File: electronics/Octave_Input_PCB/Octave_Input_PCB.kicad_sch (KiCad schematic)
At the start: 37 parts, among them SW1 SW_Hot_Swap_Socket, SW10 SW_Hot_Swap_Socket, SW11 SW_Hot_Swap_Socket, SW12 SW_Hot_Swap_Socket, SW13 SW_Hot_Swap_Socket, SW14 Alps_Alpine_RKJXV1224, SW15 Bourns_PEC12R-4xxxF-Sxxx, SW2 SW_Hot_Swap_Socket, SW3 SW_Hot_Swap_Socket, SW4 SW_Hot_Swap_Socket, SW5 SW_Hot_Swap_Socket, SW6 SW_Hot_Swap_Socket, SW7 SW_Hot_Swap_Socket, SW8 SW_Hot_Swap_Socket, SW9 SW_Hot_Swap_Socket, U1 Adafruit_QT_Py_RP2040

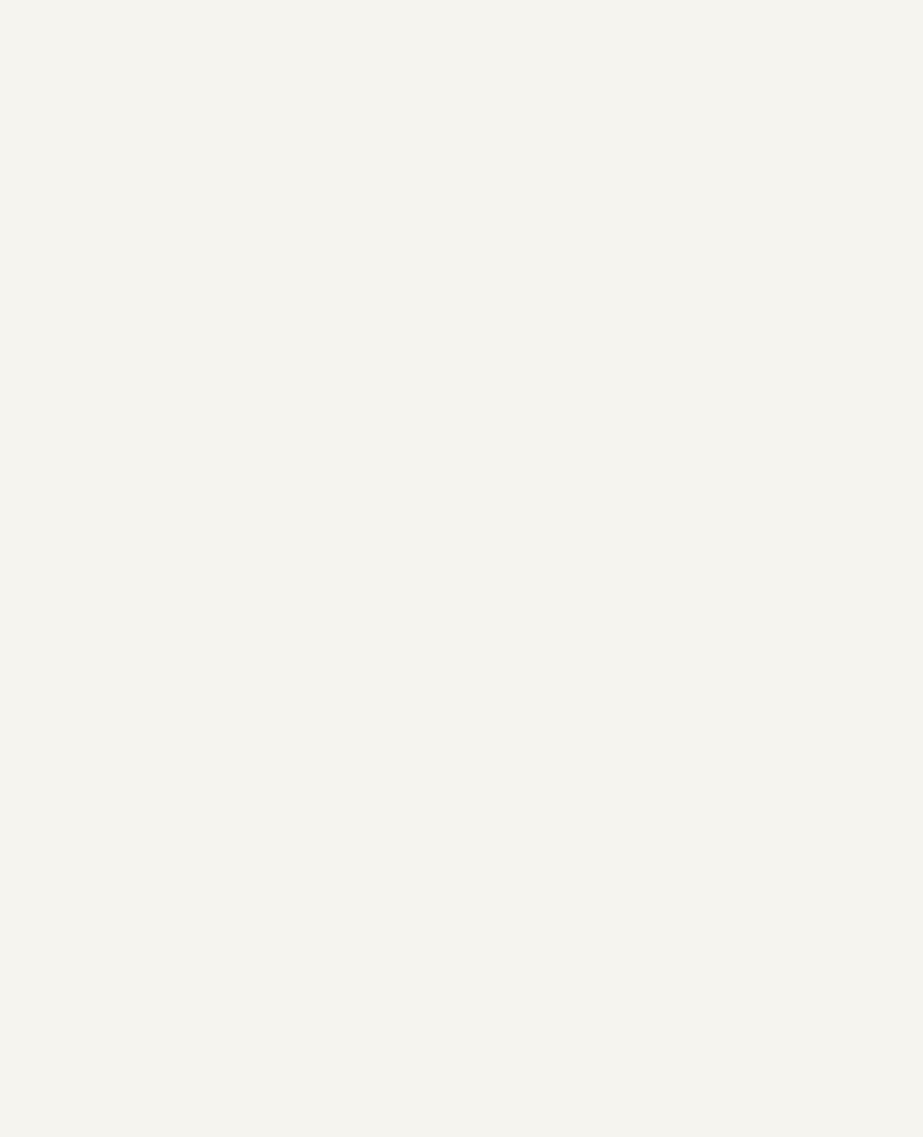
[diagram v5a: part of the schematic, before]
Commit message: Add RP2040 #schematic
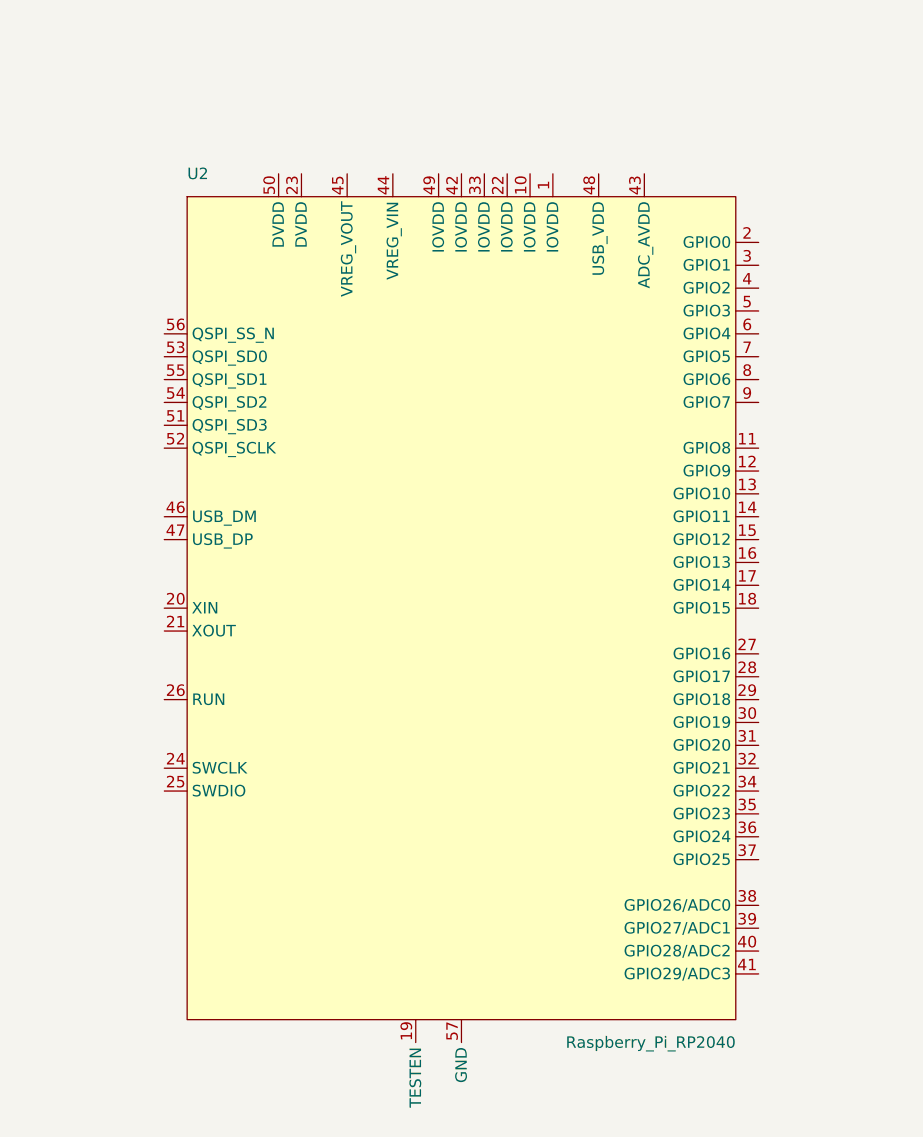
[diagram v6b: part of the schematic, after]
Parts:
- added U2: Raspberry_Pi_RP2040, Octave_Library:RP2040_QFN-56, symbol Octave_Library:Raspberry_Pi_RP2040
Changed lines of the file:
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@@
   (title_block
     (title "Octave - Input PCB")
-    (date "2022-04-29")
-    (rev "4")
+    (date "2022-05-04")
+    (rev "5.a")
     (comment 4 "https://github.com/takayoshiotake/octave-12-key-macropad")
   )
@@
   (symbol (lib_id "power:+3.3V") (at 223.52 110.49 0) (unit 1)
     (in_bom yes) (on_board yes) (fields_autoplaced)
-    (property "Reference" "#PWR?" (id 0) (at 223.52 114.3 0)
+    (property "Reference" "#PWR0102" (id 0) (at 223.52 114.3 0)
       (effects (font (size 1.27 1.27)) hide)
     )
@@
     (pin "1")
     (pin "2")
+  )
+  (symbol (lib_id "Octave_Library:Raspberry_Pi_RP2040") (at 92.71 133.35 0) (unit 1)
+    (in_bom yes) (on_board yes)
+    (property "Reference" "U2" (id 0) (at 62.23 85.09 0)
+      (effects (font (size 1.27 1.27)) (justify left))
+    )
+    (property "Value" "Raspberry_Pi_RP2040" (id 1) (at 123.19 181.61 0)
+      (effects (font (size 1.27 1.27)) (justify right))
+    )
+    (property "Footprint" "Octave_Library:RP2040_QFN-56" (id 2) (at 92.71 133.35 0)
+      (effects (font (size 1.27 1.27)) hide)
+    )
+    (property "Datasheet" "" (id 3) (at 92.71 156.21 0)
+      (effects (font (size 1.27 1.27)) hide)
+    )
+    (pin "1")
+    (pin "10")
+    (pin "11")
+    (pin "12")
+    (pin "13")
+    (pin "14")
+    (pin "15")
+    (pin "16")
+    (pin "17")
+    (pin "18")
+    (pin "19")
+    (pin "2")
+    (pin "20")
+    (pin "21")
+    (pin "22")
+    (pin "23")
+    (pin "24")
+    (pin "25")
+    (pin "26")
+    (pin "27")
+    (pin "28")
+    (pin "29")
+    (pin "3")
+    (pin "30")
+    (pin "31")
+    (pin "32")
+    (pin "33")
+    (pin "34")
+    (pin "35")
+    (pin "36")
+    (pin "37")
+    (pin "38")
+    (pin "39")
+    (pin "4")
+    (pin "40")
+    (pin "41")
+    (pin "42")
+    (pin "43")
+    (pin "44")
+    (pin "45")
+    (pin "46")
+    (pin "47")
+    (pin "48")
+    (pin "49")
+    (pin "5")
+    (pin "50")
+    (pin "51")
+    (pin "52")
+    (pin "53")
+    (pin "54")
+    (pin "55")
+    (pin "56")
+    (pin "57")
+    (pin "6")
+    (pin "7")
+    (pin "8")
+    (pin "9")
   )
   (symbol (lib_id "Diode:1N4148WS") (at 180.34 38.1 90) (unit 1)
@@
   (symbol (lib_id "power:GND") (at 218.44 115.57 0) (unit 1)
     (in_bom yes) (on_board yes) (fields_autoplaced)
-    (property "Reference" "#PWR?" (id 0) (at 218.44 121.92 0)
+    (property "Reference" "#PWR0101" (id 0) (at 218.44 121.92 0)
       (effects (font (size 1.27 1.27)) hide)
     )
@@
   (symbol (lib_id "power:+3.3V") (at 195.58 110.49 0) (unit 1)
     (in_bom yes) (on_board yes) (fields_autoplaced)
-    (property "Reference" "#PWR?" (id 0) (at 195.58 114.3 0)
+    (property "Reference" "#PWR0104" (id 0) (at 195.58 114.3 0)
       (effects (font (size 1.27 1.27)) hide)
     )
@@
   (symbol (lib_id "power:GND") (at 200.66 115.57 0) (unit 1)
     (in_bom yes) (on_board yes) (fields_autoplaced)
-    (property "Reference" "#PWR?" (id 0) (at 200.66 121.92 0)
+    (property "Reference" "#PWR0103" (id 0) (at 200.66 121.92 0)
       (effects (font (size 1.27 1.27)) hide)
     )
@@
       (reference "#PWR07") (unit 1) (value "+3.3V") (footprint "")
     )
+    (path "/95c5557f-99eb-4648-bde6-d53e11cf48f1"
+      (reference "#PWR0101") (unit 1) (value "GND") (footprint "")
+    )
     (path "/39e40374-5e2a-443a-8fbe-89eca3b36e7e"
-      (reference "#PWR?") (unit 1) (value "+3.3V") (footprint "")
-    )
-    (path "/95c5557f-99eb-4648-bde6-d53e11cf48f1"
-      (reference "#PWR?") (unit 1) (value "GND") (footprint "")
+      (reference "#PWR0102") (unit 1) (value "+3.3V") (footprint "")
+    )
+    (path "/cfa126e2-1045-4497-be93-6681d5f25665"
+      (reference "#PWR0103") (unit 1) (value "GND") (footprint "")
     )
     (path "/96c46386-d684-40bb-ae69-6b4b3b025797"
-      (reference "#PWR?") (unit 1) (value "+3.3V") (footprint "")
-    )
-    (path "/cfa126e2-1045-4497-be93-6681d5f25665"
-      (reference "#PWR?") (unit 1) (value "GND") (footprint "")
+      (reference "#PWR0104") (unit 1) (value "+3.3V") (footprint "")
     )
     (path "/172c53e1-ff21-4247-8ac3-d08b615ae4b5"
@@
       (reference "U1") (unit 1) (value "Adafruit_QT_Py_RP2040") (footprint "Octave_Library:Adafruit_QT_Py_RP2040")
     )
-  )
+    (path "/68d14432-223b-47bb-bd26-18873cfb3df2"
+      (reference "U2") (unit 1) (value "Raspberry_Pi_RP2040") (footprint "Octave_Library:RP2040_QFN-56")
+    )
+  )

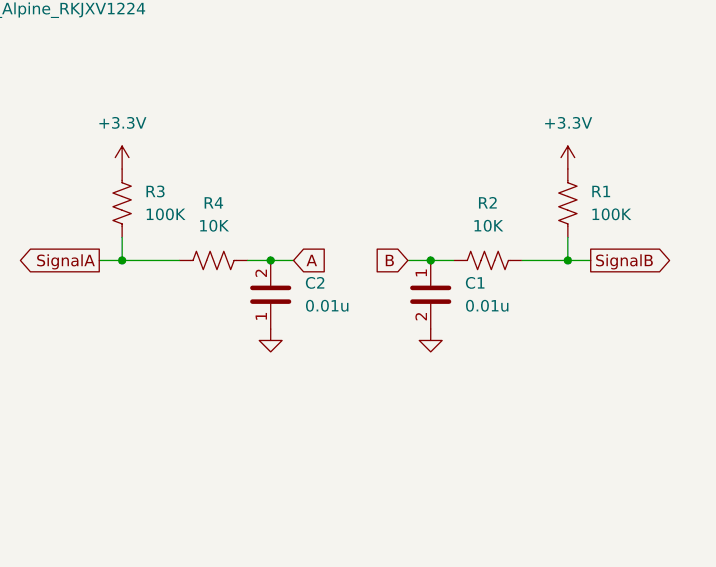
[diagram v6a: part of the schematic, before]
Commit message: Renumber the capacitors #schematic
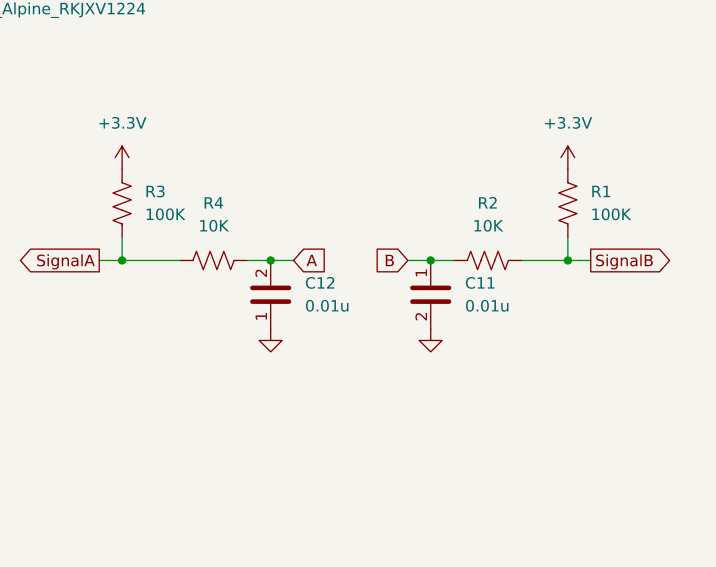
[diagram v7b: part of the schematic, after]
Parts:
- renumbered C1 to C11, C2 to C12
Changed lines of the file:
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@@
   (symbol (lib_name "C_1") (lib_id "Device:C") (at 251.46 153.67 0) (unit 1)
     (in_bom yes) (on_board yes) (fields_autoplaced)
-    (property "Reference" "C1" (id 0) (at 255.27 152.3999 0)
+    (property "Reference" "C11" (id 0) (at 255.27 152.3999 0)
       (effects (font (size 1.27 1.27)) (justify left))
     )
@@
   (symbol (lib_id "Device:C") (at 233.68 153.67 180) (unit 1)
     (in_bom yes) (on_board yes) (fields_autoplaced)
-    (property "Reference" "C2" (id 0) (at 237.49 152.3999 0)
+    (property "Reference" "C12" (id 0) (at 237.49 152.3999 0)
       (effects (font (size 1.27 1.27)) (justify right))
     )
@@
     )
     (path "/172c53e1-ff21-4247-8ac3-d08b615ae4b5"
-      (reference "C1") (unit 1) (value "0.01u") (footprint "Octave_Library:C_0805_2012Metric")
+      (reference "C11") (unit 1) (value "0.01u") (footprint "Octave_Library:C_0805_2012Metric")
     )
     (path "/21ad77bf-5ff1-4e47-a420-889e2c26128b"
-      (reference "C2") (unit 1) (value "0.01u") (footprint "Octave_Library:C_0805_2012Metric")
+      (reference "C12") (unit 1) (value "0.01u") (footprint "Octave_Library:C_0805_2012Metric")
     )
     (path "/709f02fa-f113-4f34-aada-ad74ed9e0d25"

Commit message: Change the diode footprint for the key matrix from SOD-323 to SOD-323F
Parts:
- D1, D10, D11, D12, D13, D14, D15, D2, D3, D4, D5, D6, D7, D8, D9: footprint Octave_Library:D_SOD-323 -> Octave_Library:D_SOD-323F
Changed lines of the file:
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@@
       (effects (font (size 1.27 1.27)) (justify right))
     )
-    (property "Footprint" "Octave_Library:D_SOD-323" (id 2) (at 230.505 55.88 0)
+    (property "Footprint" "Octave_Library:D_SOD-323F" (id 2) (at 230.505 55.88 0)
       (effects (font (size 1.27 1.27)) hide)
     )
@@
       (effects (font (size 1.27 1.27)) (justify right))
     )
-    (property "Footprint" "Octave_Library:D_SOD-323" (id 2) (at 215.265 55.88 0)
+    (property "Footprint" "Octave_Library:D_SOD-323F" (id 2) (at 215.265 55.88 0)
       (effects (font (size 1.27 1.27)) hide)
     )
@@
       (effects (font (size 1.27 1.27)) (justify right))
     )
-    (property "Footprint" "Octave_Library:D_SOD-323" (id 2) (at 184.785 91.44 0)
+    (property "Footprint" "Octave_Library:D_SOD-323F" (id 2) (at 184.785 91.44 0)
       (effects (font (size 1.27 1.27)) hide)
     )
@@
       (effects (font (size 1.27 1.27)) (justify right))
     )
-    (property "Footprint" "Octave_Library:D_SOD-323" (id 2) (at 215.265 38.1 0)
+    (property "Footprint" "Octave_Library:D_SOD-323F" (id 2) (at 215.265 38.1 0)
       (effects (font (size 1.27 1.27)) hide)
     )
@@
       (effects (font (size 1.27 1.27)) (justify right))
     )
-    (property "Footprint" "Octave_Library:D_SOD-323" (id 2) (at 200.025 55.88 0)
+    (property "Footprint" "Octave_Library:D_SOD-323F" (id 2) (at 200.025 55.88 0)
       (effects (font (size 1.27 1.27)) hide)
     )
@@
       (effects (font (size 1.27 1.27)) (justify right))
     )
-    (property "Footprint" "Octave_Library:D_SOD-323" (id 2) (at 200.025 38.1 0)
+    (property "Footprint" "Octave_Library:D_SOD-323F" (id 2) (at 200.025 38.1 0)
       (effects (font (size 1.27 1.27)) hide)
     )
@@
       (effects (font (size 1.27 1.27)) (justify right))
     )
-    (property "Footprint" "Octave_Library:D_SOD-323" (id 2) (at 184.785 55.88 0)
+    (property "Footprint" "Octave_Library:D_SOD-323F" (id 2) (at 184.785 55.88 0)
       (effects (font (size 1.27 1.27)) hide)
     )
@@
       (effects (font (size 1.27 1.27)) (justify right))
     )
-    (property "Footprint" "Octave_Library:D_SOD-323" (id 2) (at 196.215 99.06 0)
+    (property "Footprint" "Octave_Library:D_SOD-323F" (id 2) (at 196.215 99.06 0)
       (effects (font (size 1.27 1.27)) hide)
     )
@@
       (effects (font (size 1.27 1.27)) (justify right))
     )
-    (property "Footprint" "Octave_Library:D_SOD-323" (id 2) (at 200.025 73.66 0)
+    (property "Footprint" "Octave_Library:D_SOD-323F" (id 2) (at 200.025 73.66 0)
       (effects (font (size 1.27 1.27)) hide)
     )
@@
       (effects (font (size 1.27 1.27)) (justify right))
     )
-    (property "Footprint" "Octave_Library:D_SOD-323" (id 2) (at 184.785 38.1 0)
+    (property "Footprint" "Octave_Library:D_SOD-323F" (id 2) (at 184.785 38.1 0)
       (effects (font (size 1.27 1.27)) hide)
     )
@@
       (effects (font (size 1.27 1.27)) (justify right))
     )
-    (property "Footprint" "Octave_Library:D_SOD-323" (id 2) (at 184.785 73.66 0)
+    (property "Footprint" "Octave_Library:D_SOD-323F" (id 2) (at 184.785 73.66 0)
       (effects (font (size 1.27 1.27)) hide)
     )
@@
       (effects (font (size 1.27 1.27)) (justify right))
     )
-    (property "Footprint" "Octave_Library:D_SOD-323" (id 2) (at 230.505 73.66 0)
+    (property "Footprint" "Octave_Library:D_SOD-323F" (id 2) (at 230.505 73.66 0)
       (effects (font (size 1.27 1.27)) hide)
     )
@@
       (effects (font (size 1.27 1.27)) (justify right))
     )
-    (property "Footprint" "Octave_Library:D_SOD-323" (id 2) (at 215.265 73.66 0)
+    (property "Footprint" "Octave_Library:D_SOD-323F" (id 2) (at 215.265 73.66 0)
       (effects (font (size 1.27 1.27)) hide)
     )
@@
       (effects (font (size 1.27 1.27)) (justify right))
     )
-    (property "Footprint" "Octave_Library:D_SOD-323" (id 2) (at 255.905 91.44 0)
+    (property "Footprint" "Octave_Library:D_SOD-323F" (id 2) (at 255.905 91.44 0)
       (effects (font (size 1.27 1.27)) hide)
     )
@@
       (effects (font (size 1.27 1.27)) (justify right))
     )
-    (property "Footprint" "Octave_Library:D_SOD-323" (id 2) (at 230.505 38.1 0)
+    (property "Footprint" "Octave_Library:D_SOD-323F" (id 2) (at 230.505 38.1 0)
       (effects (font (size 1.27 1.27)) hide)
     )
@@
     )
     (path "/709f02fa-f113-4f34-aada-ad74ed9e0d25"
-      (reference "D1") (unit 1) (value "1N4148WS") (footprint "Octave_Library:D_SOD-323")
+      (reference "D1") (unit 1) (value "1N4148WS") (footprint "Octave_Library:D_SOD-323F")
     )
     (path "/3c5d03ad-ef2a-44d3-bc52-83fc5cd731c2"
-      (reference "D2") (unit 1) (value "1N4148WS") (footprint "Octave_Library:D_SOD-323")
+      (reference "D2") (unit 1) (value "1N4148WS") (footprint "Octave_Library:D_SOD-323F")
     )
     (path "/1a8ff821-98c8-41ef-919b-9109469cd4f0"
-      (reference "D3") (unit 1) (value "1N4148WS") (footprint "Octave_Library:D_SOD-323")
+      (reference "D3") (unit 1) (value "1N4148WS") (footprint "Octave_Library:D_SOD-323F")
     )
     (path "/fbe8ce2d-ce37-4567-b78b-14cbdd8d5fa9"
-      (reference "D4") (unit 1) (value "1N4148WS") (footprint "Octave_Library:D_SOD-323")
+      (reference "D4") (unit 1) (value "1N4148WS") (footprint "Octave_Library:D_SOD-323F")
     )
     (path "/4180a1a8-8e9e-403c-882e-e605ec012797"
-      (reference "D5") (unit 1) (value "1N4148WS") (footprint "Octave_Library:D_SOD-323")
+      (reference "D5") (unit 1) (value "1N4148WS") (footprint "Octave_Library:D_SOD-323F")
     )
     (path "/289a3e37-e58b-4925-9d57-18405effc2cb"
-      (reference "D6") (unit 1) (value "1N4148WS") (footprint "Octave_Library:D_SOD-323")
+      (reference "D6") (unit 1) (value "1N4148WS") (footprint "Octave_Library:D_SOD-323F")
     )
     (path "/0e2cc3b9-7e96-4254-8233-44f8db422f6e"
-      (reference "D7") (unit 1) (value "1N4148WS") (footprint "Octave_Library:D_SOD-323")
+      (reference "D7") (unit 1) (value "1N4148WS") (footprint "Octave_Library:D_SOD-323F")
     )
     (path "/053dae26-0d29-4615-8f3a-499ae7356113"
-      (reference "D8") (unit 1) (value "1N4148WS") (footprint "Octave_Library:D_SOD-323")
+      (reference "D8") (unit 1) (value "1N4148WS") (footprint "Octave_Library:D_SOD-323F")
     )
     (path "/764ac2d4-e593-4865-97ff-ed8b82b2353d"
-      (reference "D9") (unit 1) (value "1N4148WS") (footprint "Octave_Library:D_SOD-323")
+      (reference "D9") (unit 1) (value "1N4148WS") (footprint "Octave_Library:D_SOD-323F")
     )
     (path "/58bc63e9-f591-47dd-8596-d72edc57116c"
-      (reference "D10") (unit 1) (value "1N4148WS") (footprint "Octave_Library:D_SOD-323")
+      (reference "D10") (unit 1) (value "1N4148WS") (footprint "Octave_Library:D_SOD-323F")
     )
     (path "/9caea4a2-5bc1-44cc-8293-300131386895"
-      (reference "D11") (unit 1) (value "1N4148WS") (footprint "Octave_Library:D_SOD-323")
+      (reference "D11") (unit 1) (value "1N4148WS") (footprint "Octave_Library:D_SOD-323F")
     )
     (path "/870e1d5b-9785-4c66-8095-64350a305b0a"
-      (reference "D12") (unit 1) (value "1N4148WS") (footprint "Octave_Library:D_SOD-323")
+      (reference "D12") (unit 1) (value "1N4148WS") (footprint "Octave_Library:D_SOD-323F")
     )
     (path "/15dd2ce1-5057-4d96-93de-f9436edad95a"
-      (reference "D13") (unit 1) (value "1N4148WS") (footprint "Octave_Library:D_SOD-323")
+      (reference "D13") (unit 1) (value "1N4148WS") (footprint "Octave_Library:D_SOD-323F")
     )
     (path "/4a30fcaa-fa70-4ef7-bc18-1d232fee7d95"
-      (reference "D14") (unit 1) (value "1N4148WS") (footprint "Octave_Library:D_SOD-323")
+      (reference "D14") (unit 1) (value "1N4148WS") (footprint "Octave_Library:D_SOD-323F")
     )
     (path "/fbc0e23d-9856-4676-a4d7-95fcc2785fe2"
-      (reference "D15") (unit 1) (value "1N4148WS") (footprint "Octave_Library:D_SOD-323")
+      (reference "D15") (unit 1) (value "1N4148WS") (footprint "Octave_Library:D_SOD-323F")
     )
     (path "/64730bd7-54fc-4aec-9d2c-870b4ea1cdc7"
